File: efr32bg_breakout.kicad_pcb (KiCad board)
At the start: 2 copper layers, 22 x 35 mm, 12 parts, among them J1 Conn_01x06, J2 Conn_01x10, J3 Conn_01x10, U1 E104-BT53A3

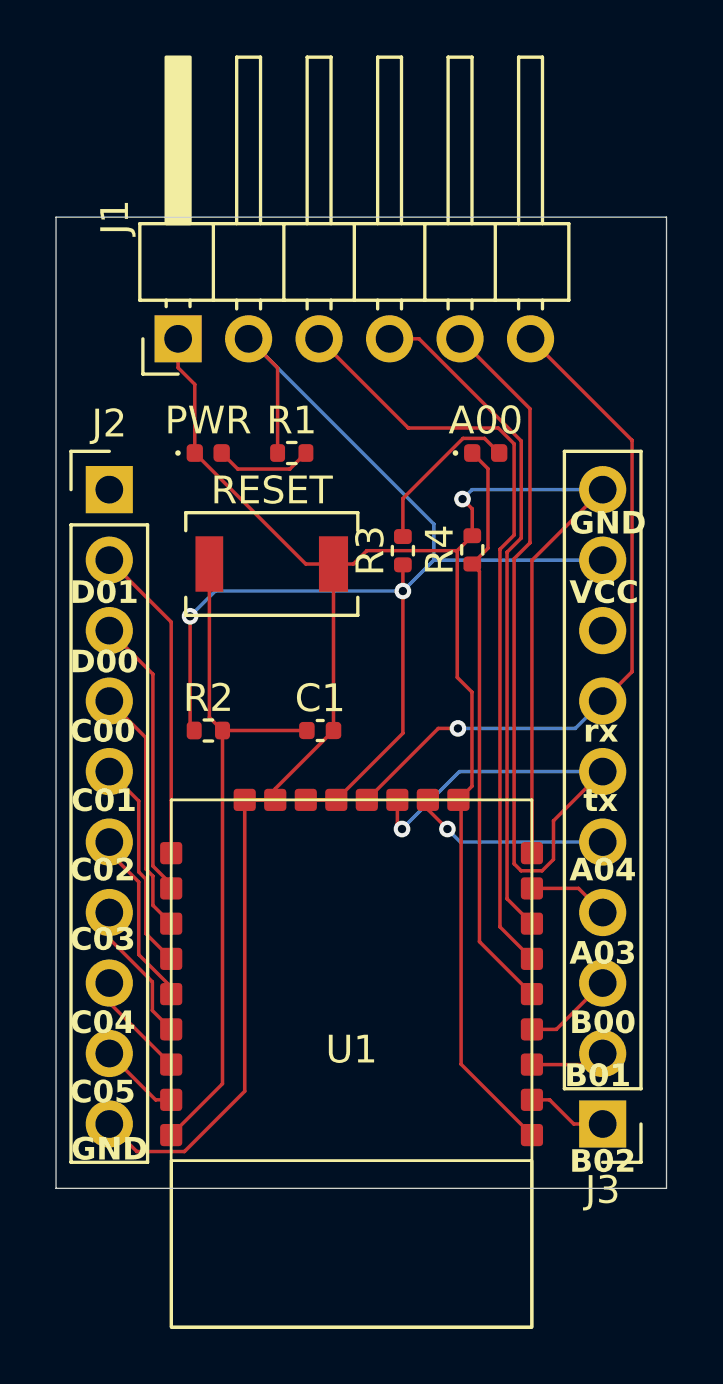
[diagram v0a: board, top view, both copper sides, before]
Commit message: use 0603 leds
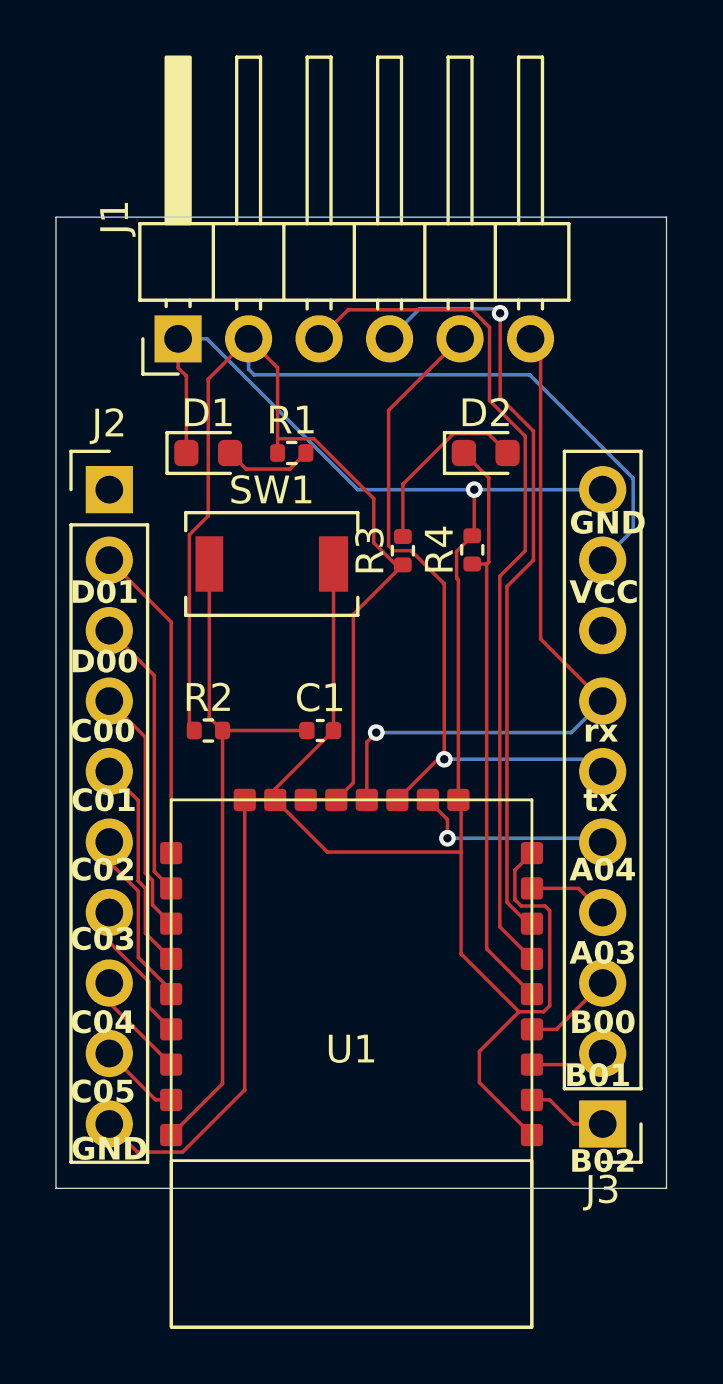
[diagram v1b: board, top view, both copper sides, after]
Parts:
- D1: renamed from PWR; footprint LED_SMD:LED_0402_1005Metric -> LED_SMD:LED_0603_1608Metric
- D2: renamed from A00; footprint LED_SMD:LED_0402_1005Metric -> LED_SMD:LED_0603_1608Metric
- renumbered RESET to SW1
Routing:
- net VCC: track 45.7 -> 57.5 mm, vias 2 -> 0
- net tx: track 36.0 -> 25.6 mm
- net swdio: track 24.2 -> 28.5 mm, vias 0 -> 1
- net GND: track 87.0 -> 90.2 mm
- net swdclk: track 27.8 -> 31.0 mm
- net Net-(D2-A): track 5.96 -> 6.70 mm
